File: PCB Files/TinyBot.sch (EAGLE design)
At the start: 11 parts

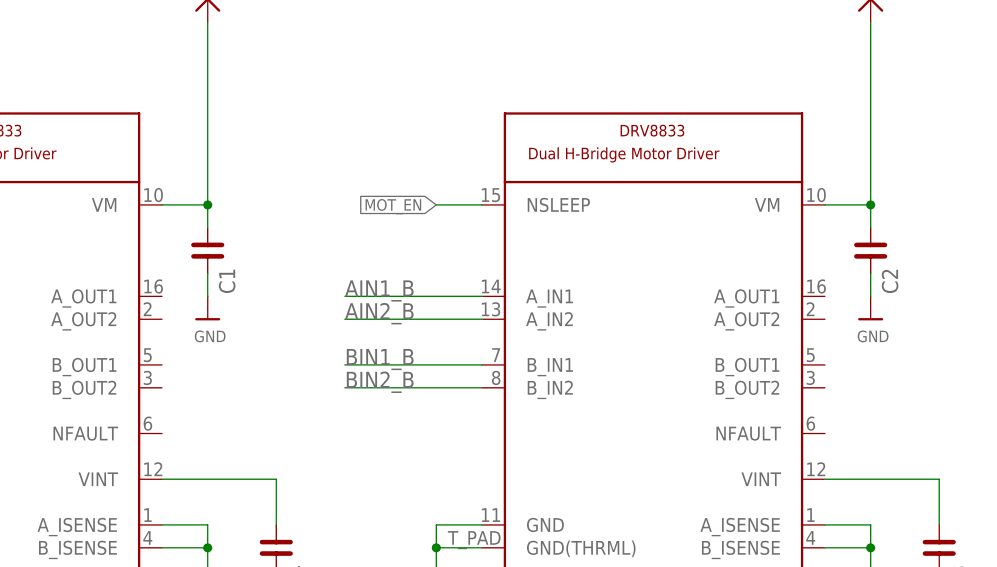
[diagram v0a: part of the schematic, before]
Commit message: PCB panel created and sent to PCBWay for review
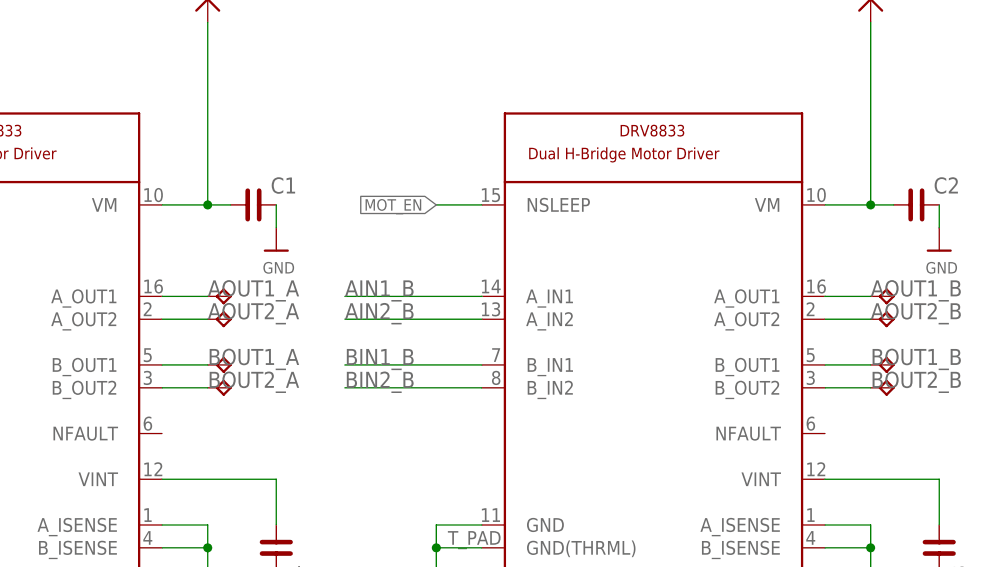
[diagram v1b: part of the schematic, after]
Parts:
- added TP1, TP2, TP3, TP4, TP5, TP6, TP7, TP8: TPTP07SQ, testpad:TPTP07SQ
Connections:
- new net AOUT1_A: TP1.TP, U$11.A_OUT1
- new net AOUT1_B: TP5.TP, U$16.A_OUT1
- new net AOUT2_A: TP2.TP, U$11.A_OUT2
- new net AOUT2_B: TP6.TP, U$16.A_OUT2
- new net BOUT1_A: TP3.TP, U$11.B_OUT1
- new net BOUT1_B: TP7.TP, U$16.B_OUT1
- new net BOUT2_A: TP4.TP, U$11.B_OUT2
- new net BOUT2_B: TP8.TP, U$16.B_OUT2
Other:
- moved on the sheet: C1, C2
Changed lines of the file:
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@@
 <part name="LIPO_IN" library="testpad" library_urn="urn:adsk.eagle:library:385" deviceset="TP" device="TP11SQ" package3d_urn="urn:adsk.eagle:package:27965/1"/>
 <part name="C5" library="rc-master-smd" deviceset="C_" device="0201"/>
+<part name="TP2" library="testpad" library_urn="urn:adsk.eagle:library:385" deviceset="TP" device="TP07SQ" package3d_urn="urn:adsk.eagle:package:27955/1"/>
+<part name="TP1" library="testpad" library_urn="urn:adsk.eagle:library:385" deviceset="TP" device="TP07SQ" package3d_urn="urn:adsk.eagle:package:27955/1"/>
+<part name="TP3" library="testpad" library_urn="urn:adsk.eagle:library:385" deviceset="TP" device="TP07SQ" package3d_urn="urn:adsk.eagle:package:27955/1"/>
+<part name="TP4" library="testpad" library_urn="urn:adsk.eagle:library:385" deviceset="TP" device="TP07SQ" package3d_urn="urn:adsk.eagle:package:27955/1"/>
+<part name="TP5" library="testpad" library_urn="urn:adsk.eagle:library:385" deviceset="TP" device="TP07SQ" package3d_urn="urn:adsk.eagle:package:27955/1"/>
+<part name="TP6" library="testpad" library_urn="urn:adsk.eagle:library:385" deviceset="TP" device="TP07SQ" package3d_urn="urn:adsk.eagle:package:27955/1"/>
+<part name="TP7" library="testpad" library_urn="urn:adsk.eagle:library:385" deviceset="TP" device="TP07SQ" package3d_urn="urn:adsk.eagle:package:27955/1"/>
+<part name="TP8" library="testpad" library_urn="urn:adsk.eagle:library:385" deviceset="TP" device="TP07SQ" package3d_urn="urn:adsk.eagle:package:27955/1"/>
 </parts>
 <sheets>
@@
 <attribute name="VALUE" x="-88.9" y="99.06" size="1.778" layer="96"/>
 </instance>
-<instance part="C1" gate="G$1" x="25.4" y="91.44" smashed="yes" rot="R270">
-<attribute name="NAME" x="26.67" y="89.535" size="1.778" layer="95" rot="R270"/>
-<attribute name="VALUE" x="21.2725" y="95.25" size="1.778" layer="96" rot="R270"/>
+<instance part="C1" gate="G$1" x="30.48" y="96.52" smashed="yes">
+<attribute name="NAME" x="32.385" y="97.79" size="1.778" layer="95"/>
+<attribute name="VALUE" x="26.67" y="92.3925" size="1.778" layer="96"/>
 </instance>
 <instance part="C4" gate="G$1" x="33.02" y="58.42" smashed="yes" rot="R270">
@@
 <attribute name="VALUE" x="-15.24" y="45.72" size="1.27" layer="95"/>
 </instance>
-<instance part="U$10" gate="G$1" x="25.4" y="83.82" smashed="yes">
-<attribute name="VALUE" x="23.876" y="81.28" size="1.27" layer="96"/>
+<instance part="U$10" gate="G$1" x="33.02" y="91.44" smashed="yes">
+<attribute name="VALUE" x="31.496" y="88.9" size="1.27" layer="96"/>
 </instance>
 <instance part="U$12" gate="G$1" x="99.06" y="119.38" smashed="yes"/>
@@
 <attribute name="VALUE" x="97.536" y="48.26" size="1.27" layer="96"/>
 </instance>
-<instance part="C2" gate="G$1" x="99.06" y="91.44" smashed="yes" rot="R270">
-<attribute name="NAME" x="100.33" y="89.535" size="1.778" layer="95" rot="R270"/>
-<attribute name="VALUE" x="94.9325" y="95.25" size="1.778" layer="96" rot="R270"/>
+<instance part="C2" gate="G$1" x="104.14" y="96.52" smashed="yes">
+<attribute name="NAME" x="106.045" y="97.79" size="1.778" layer="95"/>
+<attribute name="VALUE" x="100.33" y="92.3925" size="1.778" layer="96"/>
 </instance>
 <instance part="C3" gate="G$1" x="106.68" y="58.42" smashed="yes" rot="R270">
@@
 <attribute name="VALUE" x="58.42" y="45.72" size="1.27" layer="95"/>
 </instance>
-<instance part="U$17" gate="G$1" x="99.06" y="83.82" smashed="yes">
-<attribute name="VALUE" x="97.536" y="81.28" size="1.27" layer="96"/>
+<instance part="U$17" gate="G$1" x="106.68" y="91.44" smashed="yes">
+<attribute name="VALUE" x="105.156" y="88.9" size="1.27" layer="96"/>
 </instance>
 <instance part="U$4" gate="G$1" x="-81.28" y="68.58" smashed="yes">
@@
 <attribute name="NAME" x="-59.69" y="92.075" size="1.778" layer="95" rot="R270"/>
 <attribute name="VALUE" x="-65.0875" y="97.79" size="1.778" layer="96" rot="R270"/>
+</instance>
+<instance part="TP2" gate="G$1" x="27.94" y="83.82" smashed="yes" rot="R270">
+<attribute name="TP_SIGNAL_NAME" x="26.67" y="82.55" size="1.778" layer="97" rot="R270"/>
+</instance>
+<instance part="TP1" gate="G$1" x="27.94" y="86.36" smashed="yes" rot="R270">
+<attribute name="TP_SIGNAL_NAME" x="26.67" y="85.09" size="1.778" layer="97" rot="R270"/>
+</instance>
+<instance part="TP3" gate="G$1" x="27.94" y="78.74" smashed="yes" rot="R270">
+<attribute name="TP_SIGNAL_NAME" x="26.67" y="77.47" size="1.778" layer="97" rot="R270"/>
+</instance>
+<instance part="TP4" gate="G$1" x="27.94" y="76.2" smashed="yes" rot="R270">
+<attribute name="TP_SIGNAL_NAME" x="26.67" y="74.93" size="1.778" layer="97" rot="R270"/>
+</instance>
+<instance part="TP5" gate="G$1" x="101.6" y="86.36" smashed="yes" rot="R270">
+<attribute name="TP_SIGNAL_NAME" x="100.33" y="85.09" size="1.778" layer="97" rot="R270"/>
+</instance>
+<instance part="TP6" gate="G$1" x="101.6" y="83.82" smashed="yes" rot="R270">
+<attribute name="TP_SIGNAL_NAME" x="100.33" y="82.55" size="1.778" layer="97" rot="R270"/>
+</instance>
+<instance part="TP7" gate="G$1" x="101.6" y="78.74" smashed="yes" rot="R270">
+<attribute name="TP_SIGNAL_NAME" x="100.33" y="77.47" size="1.778" layer="97" rot="R270"/>
+</instance>
+<instance part="TP8" gate="G$1" x="101.6" y="76.2" smashed="yes" rot="R270">
+<attribute name="TP_SIGNAL_NAME" x="100.33" y="74.93" size="1.778" layer="97" rot="R270"/>
 </instance>
 </instances>
@@
 <pinref part="C1" gate="G$1" pin="2"/>
 <pinref part="U$10" gate="G$1" pin="GND"/>
-<wire x1="25.4" y1="88.9" x2="25.4" y2="86.36" width="0.1524" layer="91"/>
+<wire x1="33.02" y1="96.52" x2="33.02" y2="93.98" width="0.1524" layer="91"/>
 </segment>
 <segment>
@@
 <pinref part="C2" gate="G$1" pin="2"/>
 <pinref part="U$17" gate="G$1" pin="GND"/>
-<wire x1="99.06" y1="88.9" x2="99.06" y2="86.36" width="0.1524" layer="91"/>
+<wire x1="106.68" y1="96.52" x2="106.68" y2="93.98" width="0.1524" layer="91"/>
 </segment>
 </net>
@@
 <pinref part="U$11" gate="G$1" pin="VM"/>
 <pinref part="C1" gate="G$1" pin="1"/>
-<wire x1="25.4" y1="96.52" x2="25.4" y2="93.98" width="0.1524" layer="91"/>
+<wire x1="25.4" y1="96.52" x2="27.94" y2="96.52" width="0.1524" layer="91"/>
 <junction x="25.4" y="96.52"/>
 </segment>
@@
 <pinref part="U$16" gate="G$1" pin="VM"/>
 <pinref part="C2" gate="G$1" pin="1"/>
-<wire x1="99.06" y1="96.52" x2="99.06" y2="93.98" width="0.1524" layer="91"/>
+<wire x1="99.06" y1="96.52" x2="101.6" y2="96.52" width="0.1524" layer="91"/>
 <junction x="99.06" y="96.52"/>
 </segment>
@@
 </segment>
 </net>
+<net name="AOUT1_A" class="0">
+<segment>
+<pinref part="U$11" gate="G$1" pin="A_OUT1"/>
+<wire x1="20.32" y1="86.36" x2="25.4" y2="86.36" width="0.1524" layer="91"/>
+<pinref part="TP1" gate="G$1" pin="TP"/>
+<label x="25.4" y="86.36" size="1.778" layer="95"/>
+</segment>
+</net>
+<net name="AOUT2_A" class="0">
+<segment>
+<pinref part="U$11" gate="G$1" pin="A_OUT2"/>
+<wire x1="20.32" y1="83.82" x2="25.4" y2="83.82" width="0.1524" layer="91"/>
+<pinref part="TP2" gate="G$1" pin="TP"/>
+<label x="25.4" y="83.82" size="1.778" layer="95"/>
+</segment>
+</net>
+<net name="BOUT1_A" class="0">
+<segment>
+<pinref part="U$11" gate="G$1" pin="B_OUT1"/>
+<wire x1="20.32" y1="78.74" x2="25.4" y2="78.74" width="0.1524" layer="91"/>
+<pinref part="TP3" gate="G$1" pin="TP"/>
+<label x="25.4" y="78.74" size="1.778" layer="95"/>
+</segment>
+</net>
+<net name="BOUT2_A" class="0">
+<segment>
+<pinref part="U$11" gate="G$1" pin="B_OUT2"/>
+<wire x1="20.32" y1="76.2" x2="25.4" y2="76.2" width="0.1524" layer="91"/>
+<pinref part="TP4" gate="G$1" pin="TP"/>
+<label x="25.4" y="76.2" size="1.778" layer="95"/>
+</segment>
+</net>
+<net name="AOUT1_B" class="0">
+<segment>
+<pinref part="U$16" gate="G$1" pin="A_OUT1"/>
+<wire x1="93.98" y1="86.36" x2="99.06" y2="86.36" width="0.1524" layer="91"/>
+<pinref part="TP5" gate="G$1" pin="TP"/>
+<label x="99.06" y="86.36" size="1.778" layer="95"/>
+</segment>
+</net>
+<net name="AOUT2_B" class="0">
+<segment>
+<pinref part="U$16" gate="G$1" pin="A_OUT2"/>
+<wire x1="93.98" y1="83.82" x2="99.06" y2="83.82" width="0.1524" layer="91"/>
+<pinref part="TP6" gate="G$1" pin="TP"/>
+<label x="99.06" y="83.82" size="1.778" layer="95"/>
+</segment>
+</net>
+<net name="BOUT1_B" class="0">
+<segment>
+<pinref part="U$16" gate="G$1" pin="B_OUT1"/>
+<wire x1="93.98" y1="78.74" x2="99.06" y2="78.74" width="0.1524" layer="91"/>
+<pinref part="TP7" gate="G$1" pin="TP"/>
+<label x="99.06" y="78.74" size="1.778" layer="95"/>
+</segment>
+</net>
+<net name="BOUT2_B" class="0">
+<segment>
+<pinref part="U$16" gate="G$1" pin="B_OUT2"/>
+<wire x1="93.98" y1="76.2" x2="99.06" y2="76.2" width="0.1524" layer="91"/>
+<pinref part="TP8" gate="G$1" pin="TP"/>
+<label x="99.06" y="76.2" size="1.778" layer="95"/>
+</segment>
+</net>

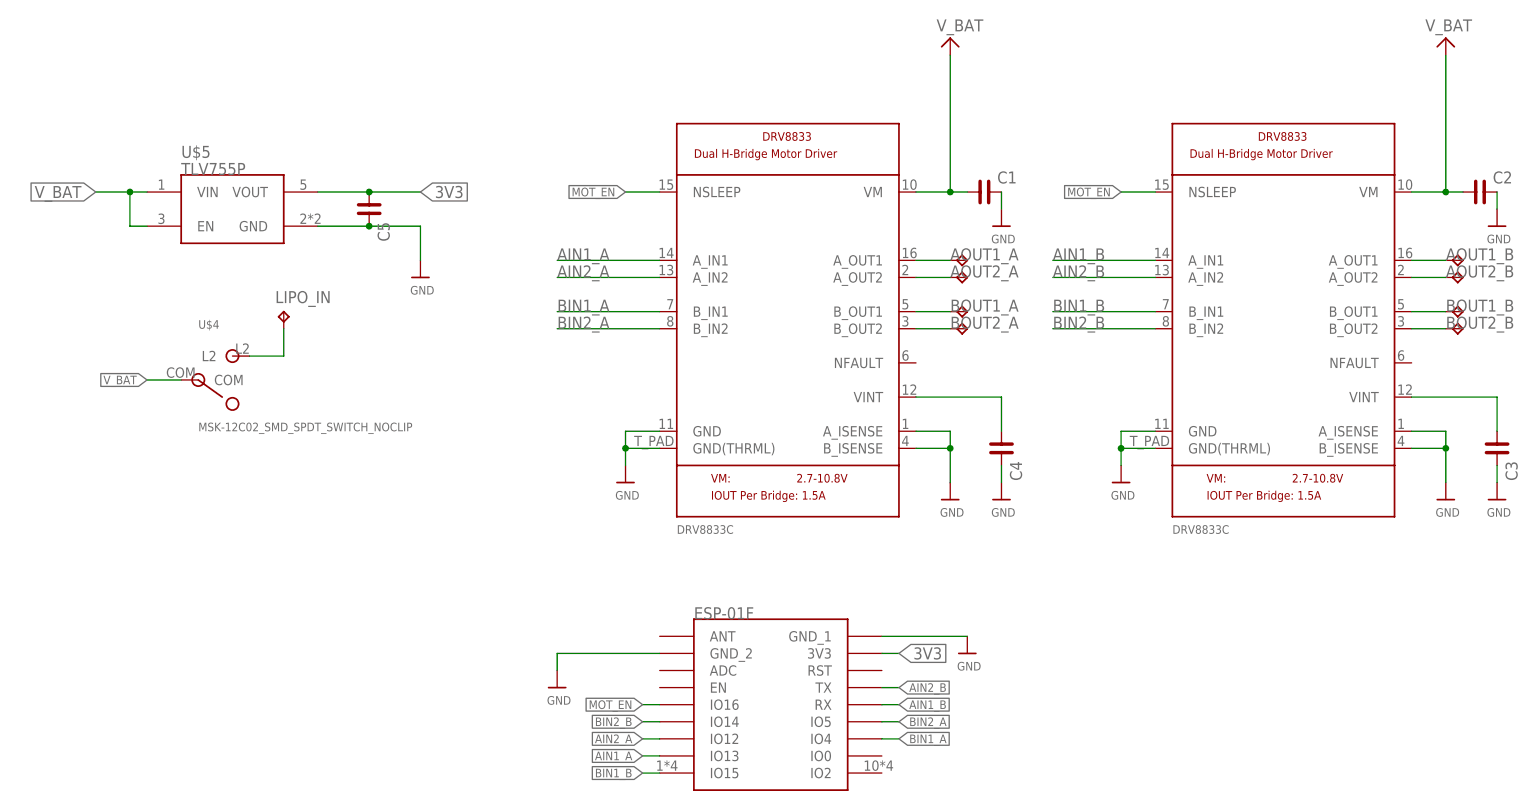
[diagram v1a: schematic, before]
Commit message: PCB first order placed, cleared PCB panel files. ESP and Python Controller software written
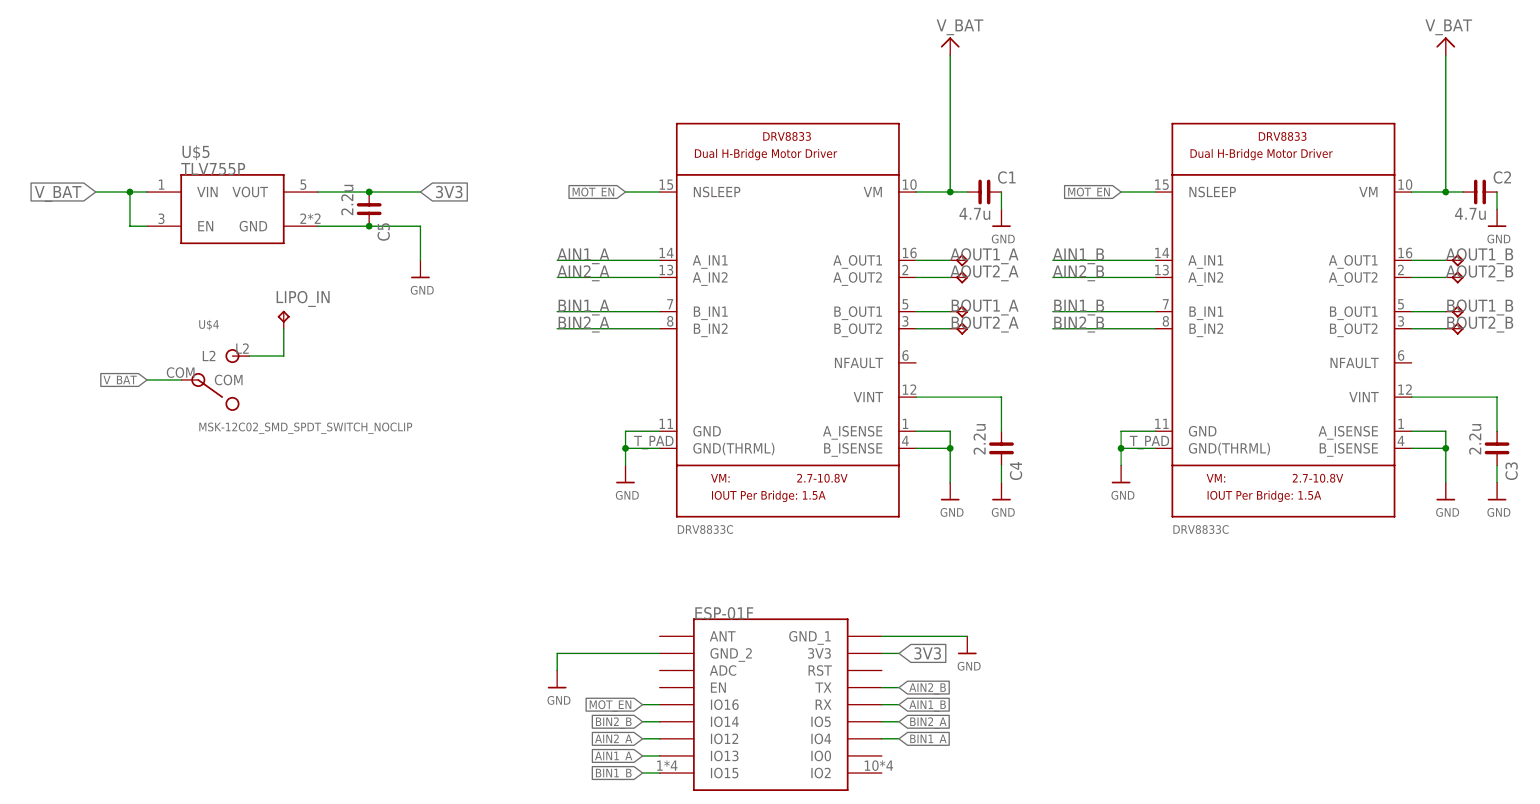
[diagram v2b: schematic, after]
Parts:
- C1, C2: value (none) -> 4.7u
- C3, C4, C5: value (none) -> 2.2u
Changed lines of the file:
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@@
 <part name="U$3" library="microbuilder" deviceset="GND" device=""/>
 <part name="U$5" library="SparkFun-IC-Power" deviceset="TLV755P" device=""/>
-<part name="C1" library="rc-master-smd" deviceset="C_" device="0201"/>
-<part name="C4" library="rc-master-smd" deviceset="C_" device="0201"/>
+<part name="C1" library="rc-master-smd" deviceset="C_" device="0201" value="4.7u"/>
+<part name="C4" library="rc-master-smd" deviceset="C_" device="0201" value="2.2u"/>
 <part name="U$6" library="microbuilder" deviceset="GND" device=""/>
 <part name="U$11" library="qfn16" deviceset="DRV8833C" device=""/>
@@
 <part name="U$14" library="microbuilder" deviceset="GND" device=""/>
 <part name="U$15" library="microbuilder" deviceset="GND" device=""/>
-<part name="C2" library="rc-master-smd" deviceset="C_" device="0201"/>
-<part name="C3" library="rc-master-smd" deviceset="C_" device="0201"/>
+<part name="C2" library="rc-master-smd" deviceset="C_" device="0201" value="4.7u"/>
+<part name="C3" library="rc-master-smd" deviceset="C_" device="0201" value="2.2u"/>
 <part name="U$16" library="qfn16" deviceset="DRV8833C" device=""/>
 <part name="U$17" library="microbuilder" deviceset="GND" device=""/>
 <part name="U$4" library="MSK-12C02 Switch SPDT" deviceset="MSK-12C02_SMD_SPDT_SWITCH_NOCLIP" device=""/>
 <part name="LIPO_IN" library="testpad" library_urn="urn:adsk.eagle:library:385" deviceset="TP" device="TP11SQ" package3d_urn="urn:adsk.eagle:package:27965/1"/>
-<part name="C5" library="rc-master-smd" deviceset="C_" device="0201"/>
+<part name="C5" library="rc-master-smd" deviceset="C_" device="0201" value="2.2u"/>
 <part name="TP2" library="testpad" library_urn="urn:adsk.eagle:library:385" deviceset="TP" device="TP07SQ" package3d_urn="urn:adsk.eagle:package:27955/1"/>
 <part name="TP1" library="testpad" library_urn="urn:adsk.eagle:library:385" deviceset="TP" device="TP07SQ" package3d_urn="urn:adsk.eagle:package:27955/1"/>
